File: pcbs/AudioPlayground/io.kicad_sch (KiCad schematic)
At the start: 30 parts, among them J1 Conn_01x05_Socket, J10 RSP-122811-01, J2 Conn_Battery, J5 Conn_01x12_Pin, J7 Conn_01x16_Pin, J9 Conn_01x05_Socket, U7 DMM-4326-T-R, U8 DMM-4326-T-R

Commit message: updated footprints, added i2s testpoints
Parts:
- J10: footprint FabisLib:SAMTEC_RSP-122811-01 -> SAMTEC_RSP-122811-01:SAMTEC_RSP-122811-01
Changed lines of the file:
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@@
 			)
 		)
-		(property "Footprint" "FabisLib:SAMTEC_RSP-122811-01"
+		(property "Footprint" "SAMTEC_RSP-122811-01:SAMTEC_RSP-122811-01"
 			(at 270.002 130.81 0)
 			(effects

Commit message: changed battery connector back to original, moved reset button so it is accessible when audio shield is on
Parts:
- J2: footprint Connector_JST:JST_PH_B2B-PH-SM4-TB_1x02-1MP_P2.00mm_Vertical -> S2B_PH_SM4_TB:JST_S2B-PH-SM4-TB
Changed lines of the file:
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@@
 			)
 		)
-		(property "Footprint" "Connector_JST:JST_PH_B2B-PH-SM4-TB_1x02-1MP_P2.00mm_Vertical"
+		(property "Footprint" "S2B_PH_SM4_TB:JST_S2B-PH-SM4-TB"
 			(at 134.62 40.64 0)
 			(effects

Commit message: Add LCSC and fix RF
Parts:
- removed AE1: 2450AT18D0100001E, 2450AT18D0100001E:2450AT18D0100001E, symbol Device:Antenna_Chip
- removed C59: 2.2pF, Capacitor_SMD:C_0402_1005Metric, symbol Device:C
- removed C61, C64: 0R, Capacitor_SMD:C_0402_1005Metric, symbol Device:C
- removed C62, C63: NC, Capacitor_SMD:C_0402_1005Metric, symbol Device:C
- removed J10: RSP-122811-01, SAMTEC_RSP-122811-01:SAMTEC_RSP-122811-01, symbol fabis_lib:RSP-122811-01
- removed L4: 4.7nH, Inductor_SMD:L_0402_1005Metric, symbol Device:L
- removed R29: 0R, Resistor_SMD:R_0402_1005Metric, symbol Device:R
- added L4: ADWH004, ADWH004:ADWH004, symbol ADWH004:ADWH004
- C44, C50: value 0.1uF -> 100nF; LCSC (none) -> C1525
- C60: value 0.7pF -> NC; MOUSER 581-04025U0R7BAT2A -> -; now not fitted; now left out of the parts list
- C65: now not fitted
- D0: value LED -> orange; LCSC (none) -> C88330
- D1: LCSC (none) -> C131223
- D2, D3: LCSC (none) -> C74338
- J1, J9: value Conn_01x05_Socket -> Conn_01x07_Socket; LCSC (none) -> C2832270
- J2: LCSC (none) -> C295747
- J5: LCSC (none) -> C7499331
- J7: LCSC (none) -> C7499334
- R23, R24, R25, R8: LCSC (none) -> C25104
- R28: value NC -> 0R; LCSC (none) -> C17168; MOUSER - -> (none); now in the parts list
- RESET1: LCSC (none) -> C231329
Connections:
- net ANT: now also C65.2, R28.1; no longer R28.2
- net at C60.2: now also R28.2, L4.1 (ANT)
- no-connect marks 1 -> 2
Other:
- note removed: "Antenna + Connector"
- note removed: "Mount either R28 or R29"

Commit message: Update MICs
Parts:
- added U19, U20: GTD3526BA-1N, GTD3526BA-1N:GTD3526BA-1N, symbol GTD3526BA-1N:GTD3526BA-1N
- U7, U8: LCSC (none) -> C47148415
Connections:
- net +3.3V: now also U19.5 (VDD), U20.2 (L/R), U20.5 (VDD)
- net DIGMICCLK: now also U19.4 (CLK), U20.4 (CLK)
- net DIGMICDATA: now also U19.1 (DATA), U20.1 (DATA)
- net GND: now also U19.2 (L/R), U19.3 (GND), U20.3 (GND)
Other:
- note added: "Note: Always only populate 2 MICs"
- moved on the sheet: C44, C50, C60, C65, L4, R28, U7, U8

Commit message: moved interface MCU LED to 3.3V switched
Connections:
- net +3.3V: no longer D0.2 (A)
- new net +3.3V_SWITCHED: D0.2 (A)
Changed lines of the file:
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@@
+	(wire
+		(pts
+			(xy 73.66 160.02) (xy 73.66 161.29)
+		)
+		(stroke
+			(width 0)
+			(type default)
+		)
+	)
 	(wire
 		(pts
@@
 	(wire
 		(pts
+			(xy 73.66 161.29) (xy 68.58 161.29)
+		)
+		(stroke
+			(width 0)
+			(type default)
+		)
+	)
+	(wire
+		(pts
 			(xy 96.52 40.64) (xy 85.09 40.64)
 		)
@@
 		(pts
 			(xy 176.53 119.38) (xy 176.53 118.11)
-		)
-		(stroke
-			(width 0)
-			(type default)
-		)
-	)
-	(wire
-		(pts
-			(xy 68.58 161.29) (xy 72.39 161.29)
 		)
 		(stroke
@@
 	)
 	(symbol
+		(lib_id "fabis_lib:3.3V_SWITCHED")
+		(at 73.66 160.02 0)
+		(unit 1)
+		(exclude_from_sim no)
+		(in_bom yes)
+		(on_board yes)
+		(dnp no)
+		(fields_autoplaced yes)
+		(property "Reference" "#PWR063"
+			(at 73.66 163.83 0)
+			(effects
+				(font
+					(size 1.27 1.27)
+				)
+				(hide yes)
+			)
+		)
+		(property "Value" "+3.3V_SWITCHED"
+			(at 73.66 154.94 0)
+			(effects
+				(font
+					(size 1.27 1.27)
+				)
+			)
+		)
+		(property "Footprint" ""
+			(at 73.66 160.02 0)
+			(effects
+				(font
+					(size 1.27 1.27)
+				)
+				(hide yes)
+			)
+		)
+		(property "Datasheet" ""
+			(at 73.66 160.02 0)
+			(effects
+				(font
+					(size 1.27 1.27)
+				)
+				(hide yes)
+			)
+		)
+		(property "Description" "Power symbol creates a global label with name \"3.3V_SWITCHED\""
+			(at 75.438 170.688 0)
+			(effects
+				(font
+					(size 1.27 1.27)
+				)
+				(hide yes)
+			)
+		)
+		(pin "1"
+		)
+		(instances
+			(project "AudioPlayground"
+				(path "/1c455b59-0247-4883-9aca-444b4cb10447/29a684ad-0419-4707-8a02-8b645f275b27"
+					(reference "#PWR063")
+					(unit 1)
+				)
+			)
+		)
+	)
+	(symbol
 		(lib_id "power:GND")
 		(at 41.91 68.58 90)
@@
 					(unit 1)
 				)
-			)
-		)
-	)
-	(symbol
-		(lib_id "power:+3.3V")
-		(at 72.39 161.29 0)
-		(unit 1)
-		(exclude_from_sim no)
-		(in_bom yes)
-		(on_board yes)
-		(dnp no)
-		(fields_autoplaced yes)
-		(property "Reference" "#PWR063"
-			(at 72.39 165.1 0)
-			(effects
-				(font
-					(size 1.27 1.27)
-				)
-				(hide yes)
-			)
-		)
-		(property "Value" "+3.3V"
-			(at 72.39 156.21 0)
-			(effects
-				(font
-					(size 1.27 1.27)
-				)
-			)
-		)
-		(property "Footprint" ""
-			(at 72.39 161.29 0)
-			(effects
-				(font
-					(size 1.27 1.27)
-				)
-				(hide yes)
-			)
-		)
-		(property "Datasheet" ""
-			(at 72.39 161.29 0)
-			(effects
-				(font
-					(size 1.27 1.27)
-				)
-				(hide yes)
-			)
-		)
-		(property "Description" "Power symbol creates a global label with name \"+3.3V\""
-			(at 72.39 161.29 0)
-			(effects
-				(font
-					(size 1.27 1.27)
-				)
-				(hide yes)
-			)
-		)
-		(pin "1"
-		)
-		(instances
-			(project "MasterProject"
-				(path "/1c455b59-0247-4883-9aca-444b4cb10447/29a684ad-0419-4707-8a02-8b645f275b27"
-					(reference "#PWR063")
-					(unit 1)
-				)

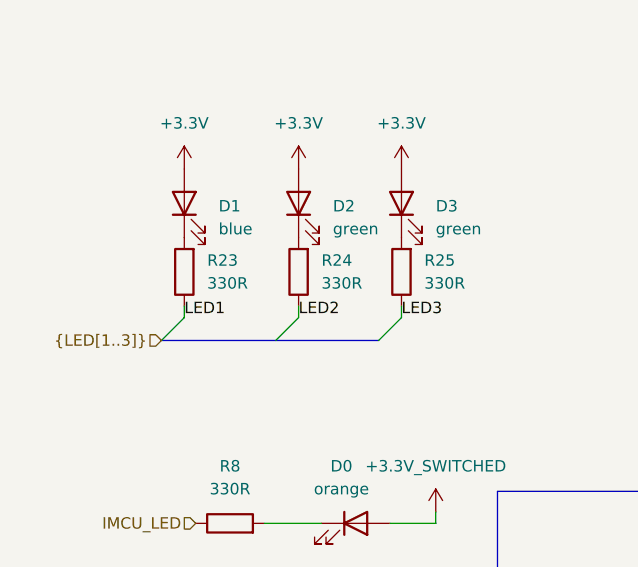
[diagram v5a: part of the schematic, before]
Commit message: Fix LED Brightness
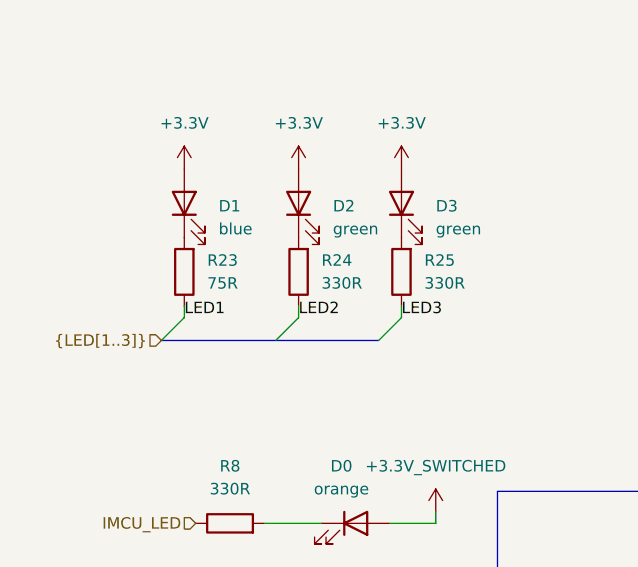
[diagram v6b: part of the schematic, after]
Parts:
- R23: value 330R -> 75R; LCSC C25104 -> C25133
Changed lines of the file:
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@@
 			)
 		)
-		(property "Value" "330R"
+		(property "Value" "75R"
 			(at 48.26 134.6199 0)
 			(effects
@@
 			)
 		)
-		(property "LCSC" "C25104"
+		(property "LCSC" " C25133"
 			(at 45.72 133.35 0)
 			(effects

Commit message: Improve Optic
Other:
- title: (none) -> LE Audio Playground
- moved on the sheet: C44, C50, C60, C65, D0, D1, D2, D3, J2, J5, J7, L4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
